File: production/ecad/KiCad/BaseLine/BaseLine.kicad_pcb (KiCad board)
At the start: 4 copper layers, 122 parts, among them IC1 AP7362-33SP-13 (3.3V LDO), J1 VibeMotorConnector_1, J10 LoadCell1, J11 LoadCell2, J12 LoadCell3, J13 LoadCell4, J14 Power_to_Loadcell, J17 IMU_connector, J2 1332645, J3 Conn_01x02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

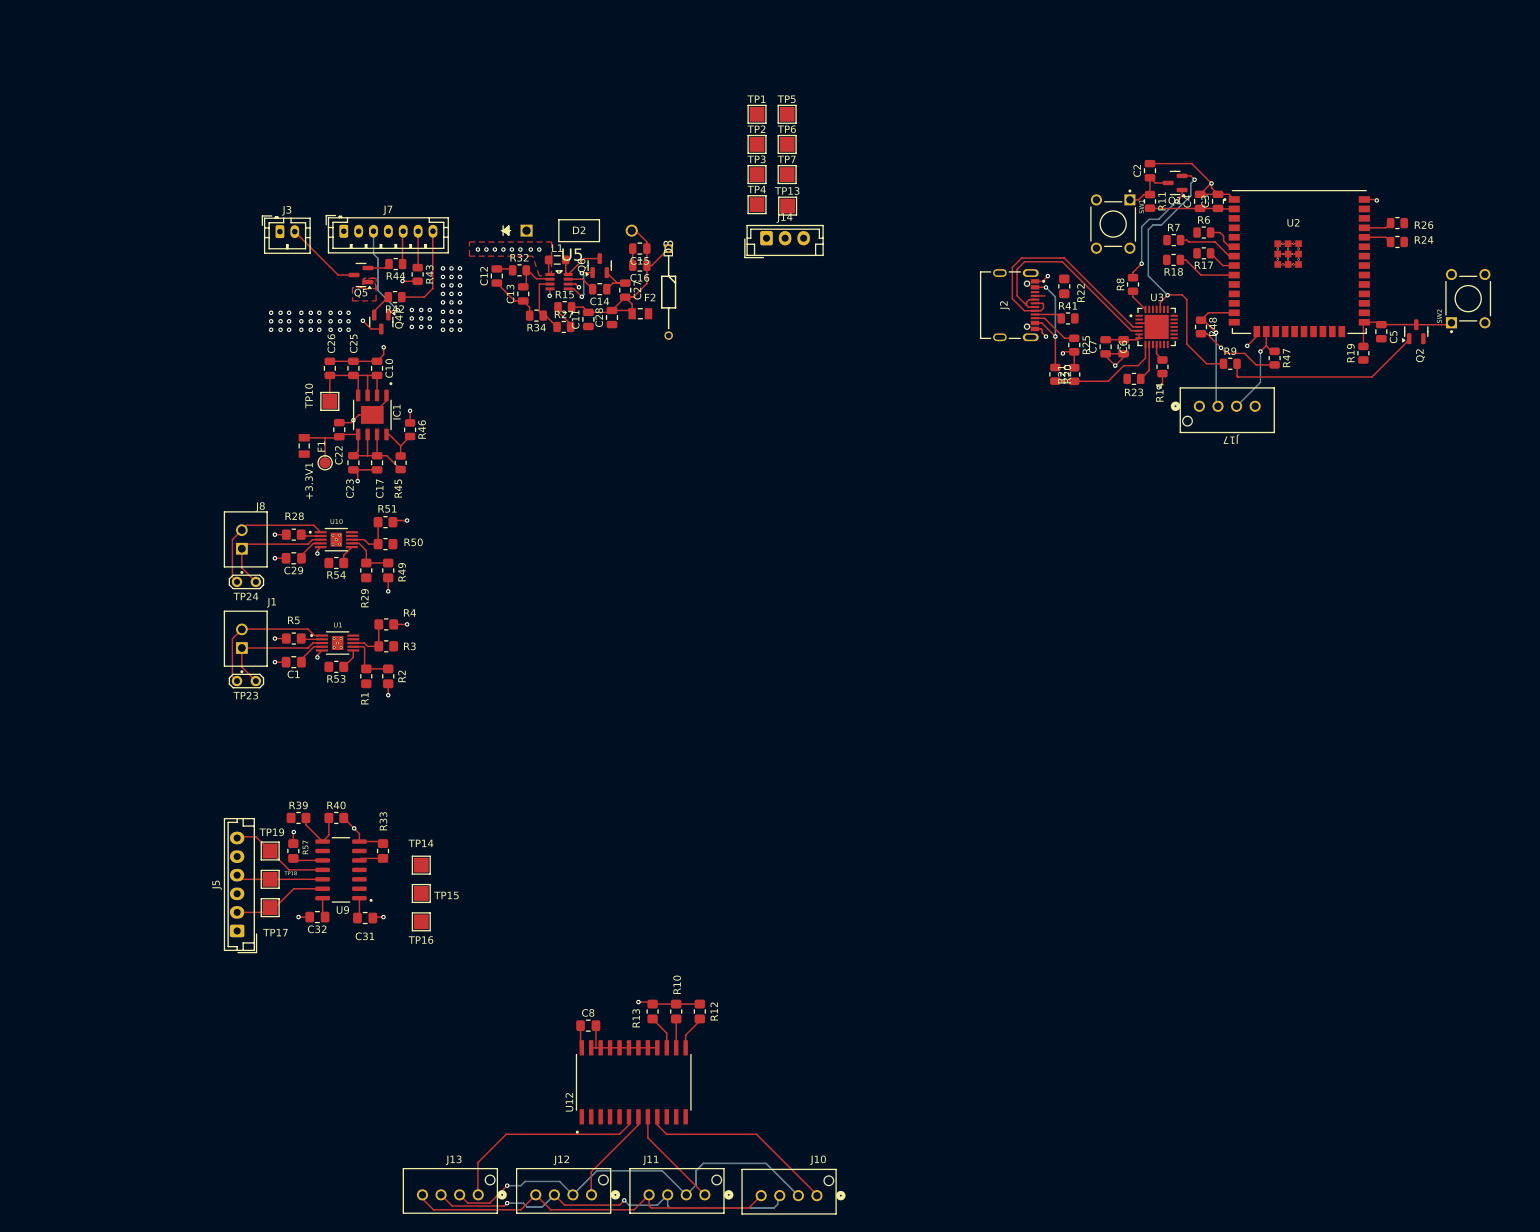
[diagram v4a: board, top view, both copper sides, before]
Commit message: Finished PCB draft 1
some errors for USBC footprint and have to fix battery connection planes
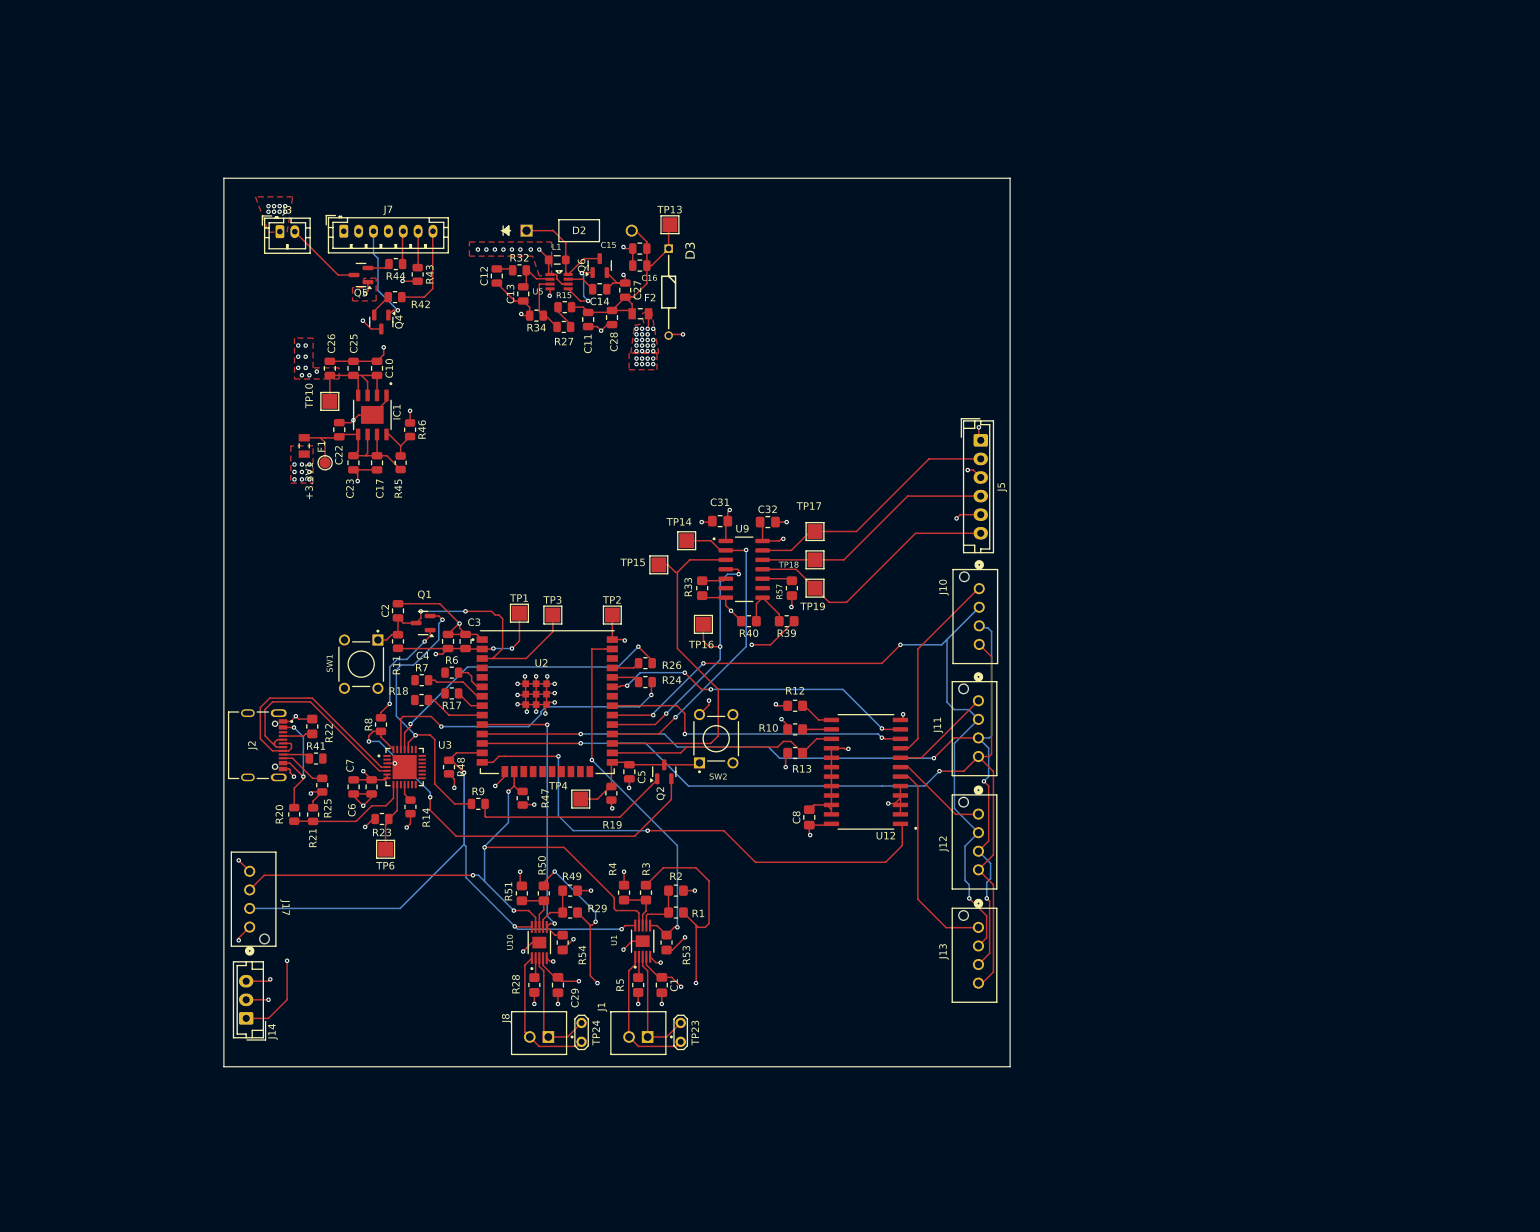
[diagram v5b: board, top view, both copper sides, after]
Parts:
- removed TP5: VRegIn, TestPoint:TestPoint_Pad_2.0x2.0mm
- removed TP7: GND, TestPoint:TestPoint_Pad_2.0x2.0mm
- moved J17 145.7 mm to (59.5, 144.2), turned to -90 degrees
- moved J14 126.1 mm to (59.0, 156.5), turned to 90 degrees
- moved J5 119.8 mm to (157.8, 78.8), turned to -90 degrees
- moved R20 118.3 mm to (65.5, 129.1)
- moved R21 118.3 mm to (68.0, 129.1)
- moved C3 117.3 mm to (88.5, 105.8)
- moved C2 117.2 mm to (79.4, 101.7)
- moved C4 117.2 mm to (86.2, 105.8)
- moved R11 117.2 mm to (79.4, 105.8)
- moved R14 117.2 mm to (81.1, 128.1)
- moved R19 117.2 mm to (108.1, 126.2)
- moved R8 117.2 mm to (77.1, 117.0)
- moved SW1 117.2 mm to (74.5, 108.9)
- moved R24 117.2 mm to (112.7, 111.3)
- moved R26 117.2 mm to (112.7, 108.7)
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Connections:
- C8 pad 2: Net-(U12-VCC) -> GND
- J3 pad 1: +3.7V -> Net-(J3-Pin_1)
- J7 pad 1: +3.7V -> Net-(J3-Pin_1)
- J7 pad 4: +3.7V -> Net-(J3-Pin_1)
- U12 pad 24: Net-(U12-VCC) -> +5V
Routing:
- net SDA: track 13.2 -> 87.7 mm, vias 1 -> 4
- net DATA_LOADCELL: track 0.00 -> 71.4 mm, vias 0 -> 2
- net SPEED: track 51.5 -> 122.2 mm, vias 0 -> 2
- net +5V: track 13.2 -> 83.5 mm, vias 0 -> 37
- net PDWN: track 51.7 -> 120.9 mm, vias 2 -> 4
- net SCL: track 17.6 -> 82.6 mm, vias 1 -> 3
- net DTR: track 3.14 -> 58.0 mm, vias 0 -> 2
- net GND: track 162.8 -> 216.2 mm, vias 30 -> 61
- net CLK: track 55.3 -> 104.7 mm, vias 1 -> 4
- net DO_rotaryenc: track 0.00 -> 49.1 mm
- net FAULTn_1: track 2.74 -> 49.7 mm, vias 0 -> 2
- net CLK_rotaryenc: track 0.00 -> 44.4 mm, vias 0 -> 2
- net MUX_SELECT_1: track 0.00 -> 42.7 mm, vias 0 -> 4
- net Net-(U3-TXD): track 0.00 -> 42.3 mm, vias 0 -> 2
- net MUX_SELECT_0: track 0.00 -> 42.2 mm, vias 0 -> 2
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- added copper zone on F.Cu, net +3.3V
- added copper zone on In1.Cu, net +3.3V
- added copper zone on F.Cu, net +5V
- added copper zone on In1.Cu, net +5V
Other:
- board outline added: 105.8 x 119.5 mm

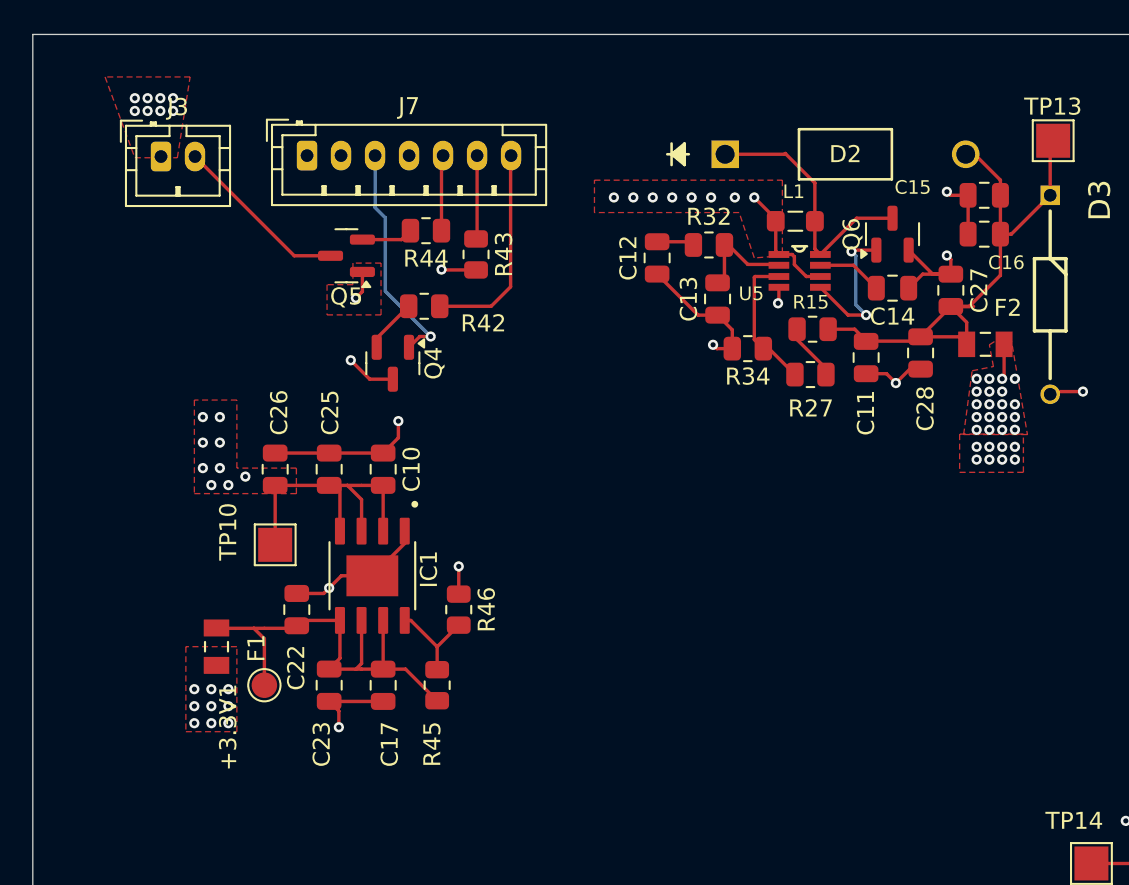
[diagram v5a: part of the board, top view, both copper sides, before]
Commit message: Added back stitching vias and fixed some routing on BMS
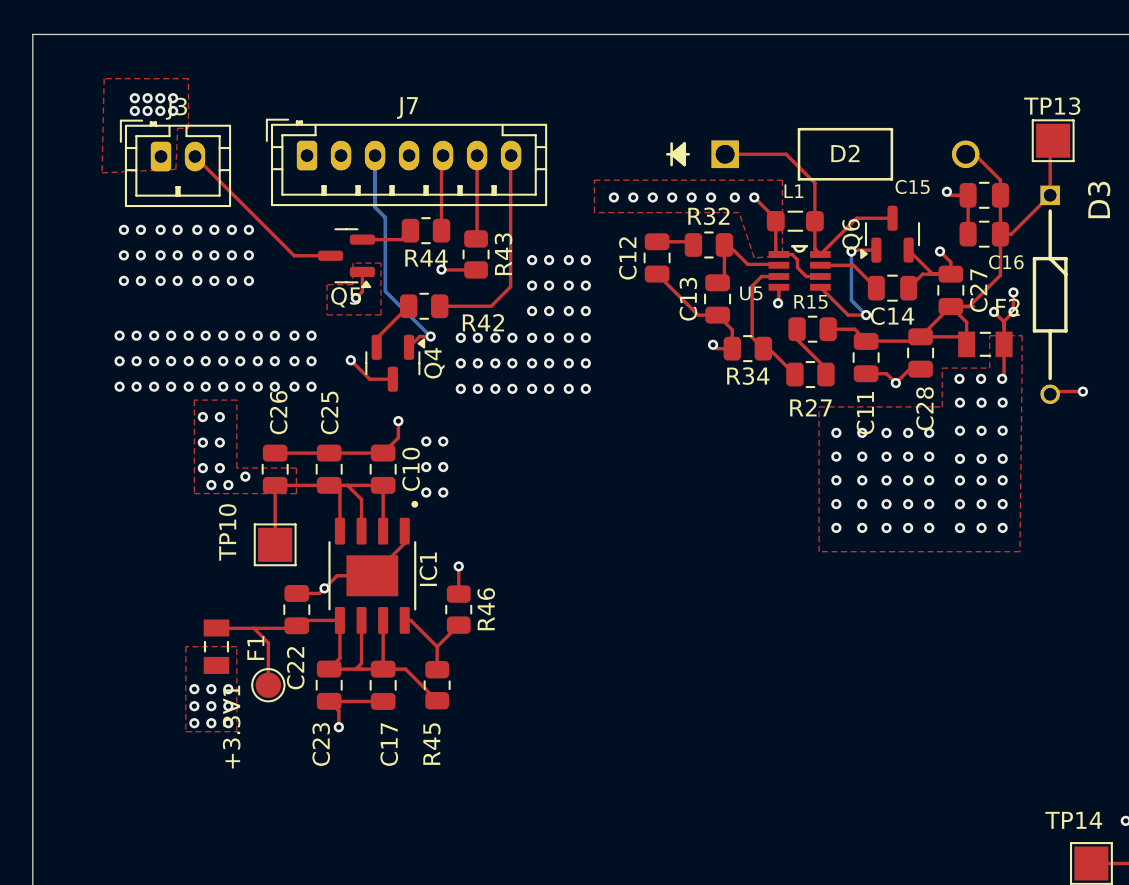
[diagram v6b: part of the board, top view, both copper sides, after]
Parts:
- moved +3.3V1 0.23 mm to (69.8, 81.8)
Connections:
- J3 pad 1: Net-(J3-Pin_1) -> +3.7V
- J7 pad 1: Net-(J3-Pin_1) -> +3.7V
- J7 pad 4: Net-(J3-Pin_1) -> +3.7V
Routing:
- net +5V: track 83.5 -> 87.9 mm, vias 37 -> 59
- net +3.7V: vias 26 -> 128

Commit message: Changed power planes and vias
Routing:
- net +5V: vias 59 -> 42
- net +3.7V: vias 128 -> 82

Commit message: Updated vias and power planes
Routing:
- net Net-(D2A-K): track 35.1 -> 33.8 mm
- net +3.7V: vias 82 -> 84
- net GND: vias 61 -> 66
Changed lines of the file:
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@@
 	)
 	(segment
+		(start 76.0305 75.2685)
+		(end 75.967 75.332)
+		(width 0.2)
+		(layer "F.Cu")
+		(net 3)
+	)
+	(segment
 		(start 96.49 113)
 		(end 96.6 112.89)
@@
 	(segment
 		(start 77.872 73.427)
-		(end 75.967 75.332)
+		(end 76.0305 75.2685)
 		(width 0.2)
 		(layer "F.Cu")
@@
 	)
 	(via
+		(at 76.835 74.803)
+		(size 0.6)
+		(drill 0.3)
+		(layers "F.Cu" "B.Cu")
+		(net 3)
+	)
+	(via
 		(at 98 115.25)
 		(size 0.6)
@@
 	)
 	(via
+		(at 76.0305 75.2685)
+		(size 0.6)
+		(drill 0.3)
+		(layers "F.Cu" "B.Cu")
+		(net 3)
+	)
+	(via
 		(at 109.75 52.75)
 		(size 0.6)
@@
 	)
 	(via
+		(at 76.835 76.073)
+		(size 0.6)
+		(drill 0.3)
+		(layers "F.Cu" "B.Cu")
+		(net 3)
+	)
+	(via
 		(at 100.5 111.5)
 		(size 0.6)
@@
 	)
 	(via
+		(at 75.184 75.946)
+		(size 0.6)
+		(drill 0.3)
+		(layers "F.Cu" "B.Cu")
+		(net 3)
+	)
+	(via
 		(at 130.25 114.25)
 		(size 0.6)
@@
 	)
 	(via
+		(at 75.184 74.803)
+		(size 0.6)
+		(drill 0.3)
+		(layers "F.Cu" "B.Cu")
+		(net 3)
+	)
+	(via
 		(at 87.702 103.391)
 		(size 0.6)
@@
 	)
 	(segment
-		(start 75.382 57.465)
-		(end 75.382 58.618)
+		(start 74.5 70.017)
+		(end 75.332 70.017)
 		(width 0.2)
 		(layer "F.Cu")
@@
 	)
 	(segment
-		(start 74.5 70.017)
-		(end 75.332 70.017)
+		(start 75.184 59.055)
+		(end 75.382 58.857)
 		(width 0.2)
 		(layer "F.Cu")
@@
 	)
 	(segment
-		(start 75.382 58.618)
-		(end 75 59)
-		(width 0.2)
-		(layer "F.Cu")
-		(net 7)
-	)
-	(segment
 		(start 100.965 57.215)
 		(end 100.965 56.7532)
@@
 		(net 7)
 	)
+	(segment
+		(start 75.382 58.857)
+		(end 75.382 57.465)
+		(width 0.2)
+		(layer "F.Cu")
+		(net 7)
+	)
 	(via
 		(at 85.725 59.769)
@@
 	)
 	(via
-		(at 62.75 48)
+		(at 62.357 48.006)
 		(size 0.6)
 		(drill 0.3)
@@
 	)
 	(via
+		(at 74.041 59.055)
+		(size 0.6)
+		(drill 0.3)
+		(layers "F.Cu" "B.Cu")
+		(free yes)
+		(net 7)
+	)
+	(via
 		(at 63.135 64.214)
 		(size 0.6)
@@
 	)
 	(via
-		(at 62 47.25)
+		(at 61.214 46.99)
 		(size 0.6)
 		(drill 0.3)
@@
 	)
 	(via
-		(at 75 59)
+		(at 75.184 59.055)
 		(size 0.6)
 		(drill 0.3)
@@
 	)
 	(via
-		(at 62 48)
+		(at 61.214 48.006)
 		(size 0.6)
 		(drill 0.3)
@@
 	)
 	(via
-		(at 63.5 47.25)
+		(at 63.5 46.99)
 		(size 0.6)
 		(drill 0.3)
@@
 	)
 	(via
-		(at 62.75 47.25)
+		(at 62.357 46.99)
 		(size 0.6)
 		(drill 0.3)
@@
 	)
 	(via
-		(at 64.25 48)
+		(at 64.643 48.133)
 		(size 0.6)
 		(drill 0.3)
@@
 	)
 	(via
+		(at 76.327 59.055)
+		(size 0.6)
+		(drill 0.3)
+		(layers "F.Cu" "B.Cu")
+		(free yes)
+		(net 7)
+	)
+	(via
 		(at 66 69)
 		(size 0.6)
@@
 	)
 	(via
-		(at 64.25 47.25)
+		(at 64.516 46.99)
 		(size 0.6)
 		(drill 0.3)
@@
 	)
 	(segment
-		(start 109.982 59.497)
-		(end 111.318 59.497)
-		(width 0.2)
-		(layer "F.Cu")
-		(net 8)
-	)
-	(segment
 		(start 110.914 61.722)
 		(end 110.472 61.28)
@@
 		(polygon
 			(pts
-				(xy 65 84.5) (xy 68 84.5) (xy 68 79.5) (xy 65 79.5)
+				(xy 64.619 84.627) (xy 68 84.5) (xy 68 79.5) (xy 64.619 79.627)
 			)
 		)
